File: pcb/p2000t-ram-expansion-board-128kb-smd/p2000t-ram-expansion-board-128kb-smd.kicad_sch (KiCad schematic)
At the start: 23 parts, among them J1 EXPANSION BOARD, J2 POWER, J3 TERMINAL, U1 74HC04, U2 CY62256-70PC, U3 74HC00, U4 CY62256-70PC, U5 74HC688, U6 74HC32, U7 74HC173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

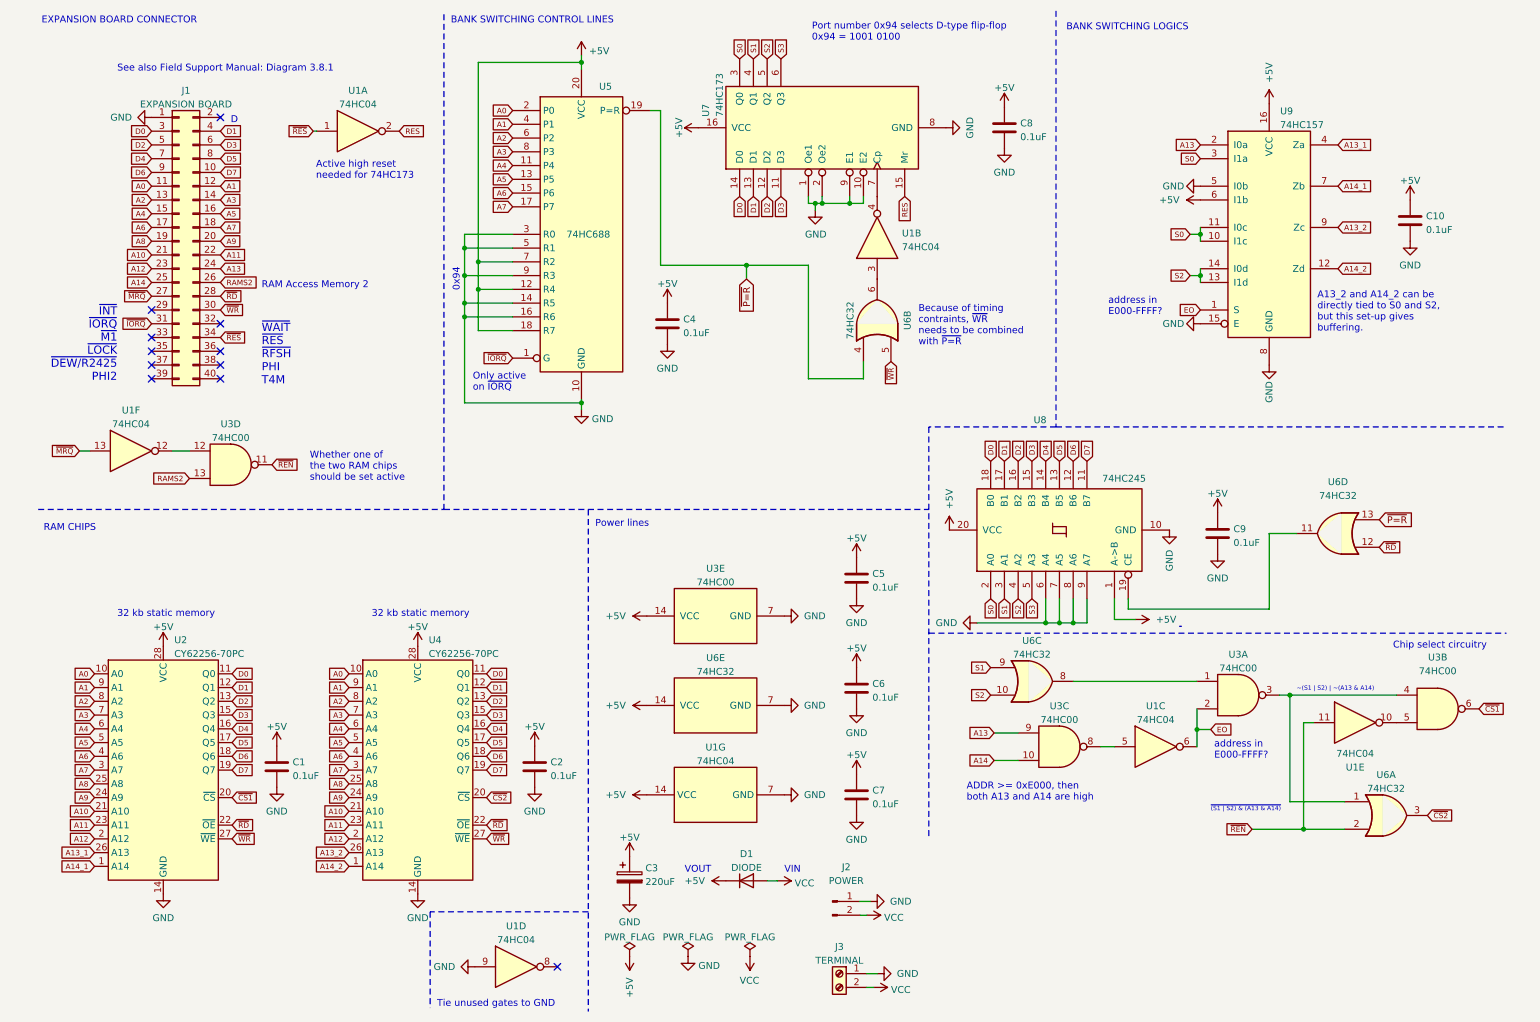
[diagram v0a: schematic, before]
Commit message: Adding 128KiB SMD design
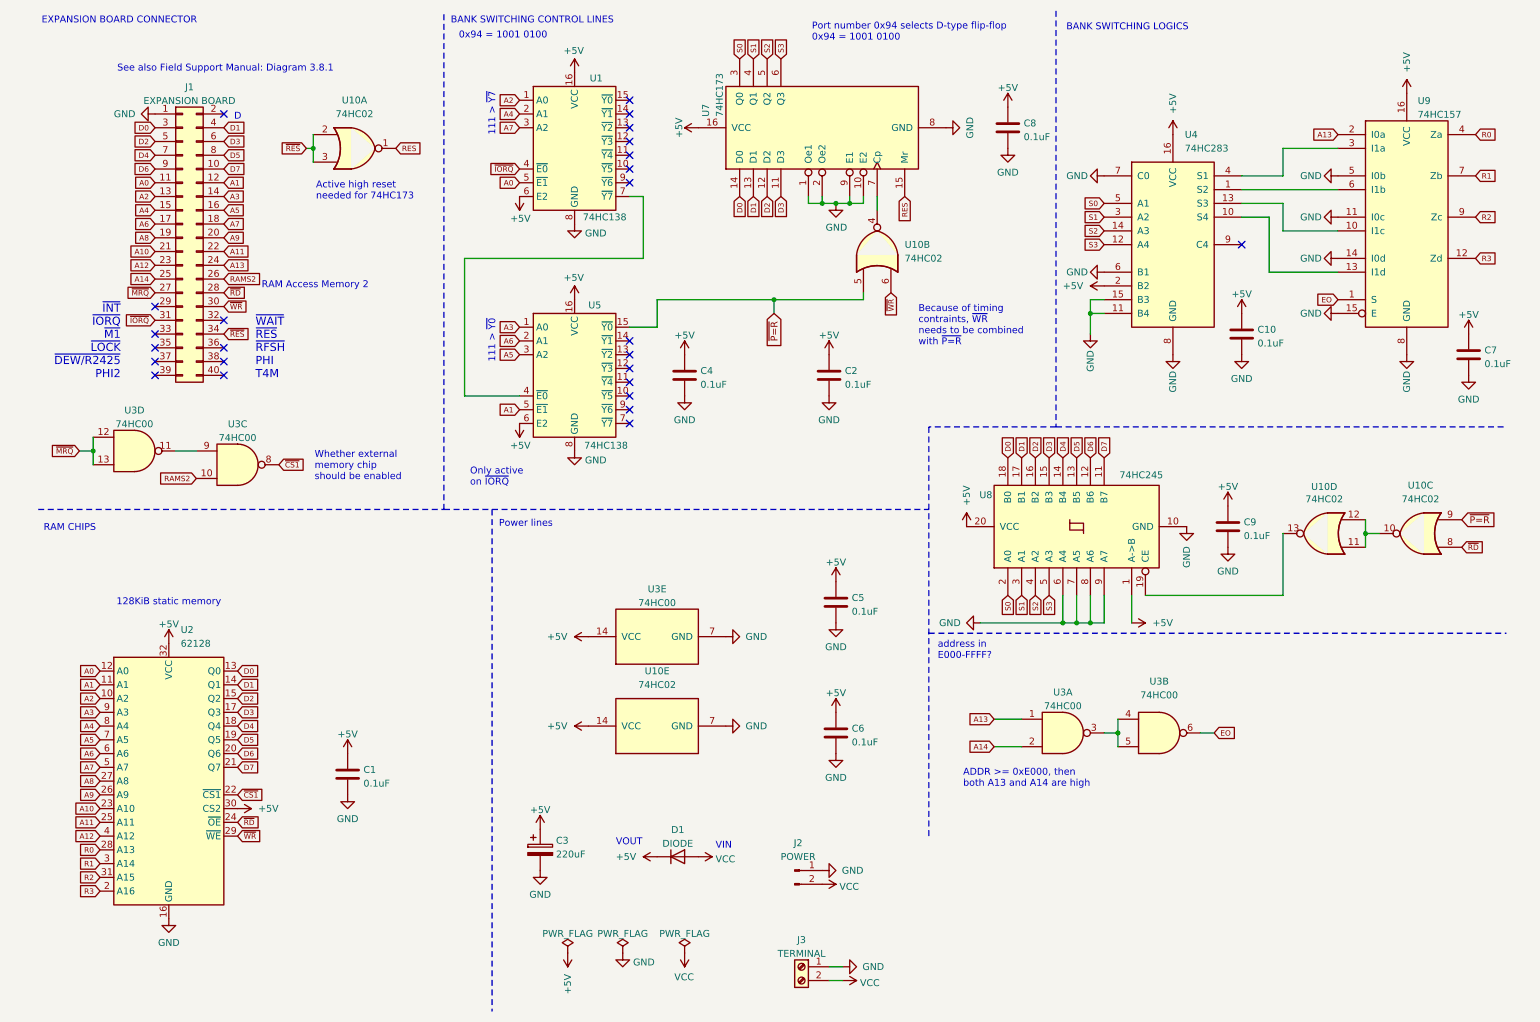
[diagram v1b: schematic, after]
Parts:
- removed J2: POWER, Connector_PinHeader_2.54mm:PinHeader_1x02_P2.54mm_Vertical, symbol Connector:Conn_01x02_Male
- removed U1: 74HC04, Package_DIP:DIP-14_W7.62mm_Socket, symbol 74xx:74HC04
- removed U2, U4: CY62256-70PC, Package_DIP:DIP-28_W15.24mm_Socket, symbol Memory_RAM:CY62256-70PC
- removed U5: 74HC688, Package_DIP:DIP-20_W7.62mm_Socket, symbol 74xx:74LS688
- removed U6: 74HC32, Package_DIP:DIP-14_W7.62mm_Socket, symbol 74xx:74LS32
- added J2: POWER, Connector_PinSocket_2.54mm:PinSocket_1x02_P2.54mm_Vertical, symbol Connector:Conn_01x02_Pin
- added U1, U5: 74HC138, Package_SO:SOIC-16_3.9x9.9mm_P1.27mm, symbol 74xx:74HC138
- added U10: 74HC02, Package_SO:SOIC-14_3.9x8.7mm_P1.27mm, symbol 74xx:74HC02
- added U2: 62128, Package_SO:SSOP-32_11.305x20.495mm_P1.27mm, symbol Memory_RAM:628128_DIP32_SSOP32
- added U4: 74HC283, Package_SO:SOIC-16_3.9x9.9mm_P1.27mm, symbol 74xx:74LS283
- C1, C10, C2, C4, C5, C6, C7, C8, C9: footprint Capacitor_THT:C_Disc_D5.0mm_W2.5mm_P5.00mm -> Capacitor_SMD:C_0805_2012Metric_Pad1.18x1.45mm_HandSolder; LCSC Part # (none) -> C126469
- U3: footprint Package_DIP:DIP-14_W7.62mm_Socket -> Package_SO:SOIC-14_3.9x8.7mm_P1.27mm; LCSC Part # (none) -> C699445
- U7: footprint Package_DIP:DIP-16_W7.62mm_Socket -> Package_SO:SOIC-16_3.9x9.9mm_P1.27mm; LCSC Part # (none) -> C546651
- U8: footprint Package_DIP:DIP-20_W7.62mm_Socket -> Package_SO:SOIC-20W_7.5x12.8mm_P1.27mm; LCSC Part # (none) -> C5625
- U9: footprint Package_DIP:DIP-16_W7.62mm_Socket -> Package_SO:SOIC-16_3.9x9.9mm_P1.27mm; LCSC Part # (none) -> C6823
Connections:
- net +5V: now also U1.16 (VCC), U1.6 (E2), U10.14 (VCC), U2.30 (CS2), U2.32 (VCC), U4.16 (VCC), U4.2 (B2), U5.16 (VCC), U5.6 (E2); no longer U9.6 (I1b)
- net A0: now also U1.5 (~{E1}), U2.12 (A0)
- net A1: now also U2.11 (A1), U5.5 (~{E1})
- net A10: now also U2.23 (A10)
- net A11: now also U2.25 (A11)
- net A12: now also U2.4 (A12)
- net A13: now also U3.1; no longer U3.9
- net A14: now also U3.2; no longer U3.10
- net A2: now also U1.1 (A0), U2.10 (A2)
- net A3: now also U2.9 (A3), U5.1 (A0)
- net A4: now also U1.2 (A1), U2.8 (A4)
- net A5: now also U2.7 (A5), U5.3 (A2)
- net A6: now also U2.6 (A6), U5.2 (A1)
- net A7: now also U1.3 (A2), U2.5 (A7)
- net A8: now also U2.27 (A8)
- net A9: now also U2.26 (A9)
- net D0: now also U2.13 (Q0)
- net D1: now also U2.14 (Q1)
- net D2: now also U2.15 (Q2)
- net D3: now also U2.17 (Q3)
- net D4: now also U2.18 (Q4)
- net D5: now also U2.19 (Q5)
- net D6: now also U2.20 (Q6)
- net D7: now also U2.21 (Q7)
- net EO: now also U3.6; no longer U3.2
- net GND: now also U9.11 (I0c), U9.14 (I0d), J2.1 (Pin_1), U1.8 (GND), U10.7 (GND), U2.16 (GND), U4.11 (B4), U4.15 (B3), U4.6 (B1), U4.7 (C0), U4.8 (GND), U5.8 (GND)
- net RAMS2: now also U3.10; no longer U3.13
- net RES: now also U10.1
- net S0: now also U4.5 (A1); no longer U9.10 (I1c), U9.11 (I0c), U9.3 (I1a)
- net S1: now also U4.3 (A2)
- net S2: now also U4.14 (A3); no longer U9.13 (I1d), U9.14 (I0d)
- net S3: now also U4.12 (A4)
- net VCC: now also J2.2 (Pin_2)
- net ~{CS1}: now also U3.8, U2.22 (~{CS1}); no longer U3.6
- net ~{IORQ}: now also U1.4 (~{E0})
- net ~{MRQ}: now also U3.12, U3.13
- net ~{P=R}: now also U10.5, U10.9, U5.15 (~{Y0})
- net ~{RD}: now also U10.8, U2.24 (~{OE})
- net ~{RES}: now also U10.2, U10.3
- net ~{WR}: now also U10.6, U2.29 (~{WE})
- net at U3.3, U3.4: now also U3.5
- net at U7.7 (Cp): now also U10.4
- net at U8.19 (CE): now also U10.13
- net A13_1 renamed R0
- net R0: now also U2.28 (A13)
- net A13_2 renamed R2
- net R2: now also U2.31 (A15)
- net A14_1 renamed R1
- net R1: now also U2.3 (A14)
- net A14_2 renamed R3
- net R3: now also U2.2 (A16)
- net ~{REN}: no longer names the net of U3.11
- net ~{REN}: now also U3.9
- new net: U4.1 (S2), U9.6 (I1b)
- new net: U4.10 (S4), U9.13 (I1d)
- new net: U4.13 (S3), U9.10 (I1c)
- new net: U4.4 (S1), U9.3 (I1a)
- new net: U10.10, U10.11, U10.12
- new net: U1.7 (~{Y7}), U5.4 (~{E0})
- no-connect marks 11 -> 25
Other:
- note added: "0x94 = 1001 0100"
- note added: "111 > ~{Y0}"
- note added: "111 > ~{Y7}"
- note added: "128KiB static memory"
- note added: "Whether external memory chip should be enabled"
- note removed: "0x94"
- note removed: "32 kb static memory"
- note removed: "A13_2 and A14_2 can be directly tied to S0 and S2, but this set-up gives buffering."
- note removed: "Chip select circuitry"
- note removed: "Tie unused gates to GND"
- note removed: "Whether one of the two RAM chips should be set active"
- note removed: "~(S1 | S2) | ~(A13 & A14)"
- note removed: "~{(S1 | S2) & (A13 & A14)}"
- title: Philips P2000T 64kb memory expansion board -> Philips P2000T 128KiB memory expansion board (SMD)
- moved on the sheet: C1, C10, C3, C4, C5, C6, C7, C8, C9, D1, J1, J3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

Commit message: Saving schematic
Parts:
- D1: value DIODE -> 1N4148
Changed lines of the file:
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@@
 		(fields_autoplaced yes)
 		(property "Reference" "D1"
-			(at 130.81 163.9402 0)
+			(at 130.81 162.56 0)
 			(effects
 				(font
@@
 			)
 		)
-		(property "Value" "DIODE"
-			(at 130.81 166.4771 0)
+		(property "Value" "1N4148"
+			(at 130.81 165.1 0)
 			(effects
 				(font
